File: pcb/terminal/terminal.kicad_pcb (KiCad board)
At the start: 2 copper layers, 34 parts, among them J1 Conn_02x08_Odd_Even, Q1 2N7002, Q2 2N7002, Q3 2N7002, SW1 1, SW10 8, SW11 9, SW13 0, SW2 2, SW3 3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

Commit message: Updates
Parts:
- added C2: 0.1u, Capacitor_SMD:C_0805_2012Metric_Pad1.15x1.40mm_HandSolder, F.Cu at (150.5, 60.0)
- added D14: 1N5818, Diode_THT:D_DO-41_SOD81_P10.16mm_Horizontal, F.Cu at (134.0, 58.0)
- added J2: ISP, Connector_PinHeader_2.54mm:PinHeader_2x03_P2.54mm_Vertical, F.Cu at (154.5, 67.5)
- added U1: ATtiny88, Package_DIP:DIP-28_W7.62mm, F.Cu at (139.5, 42.5)
- C1: value 0.47u -> 47u
- J1: value Conn_02x08_Odd_Even -> Conn_02x15_Odd_Even; footprint Connector_IDC:IDC-Header_2x08_P2.54mm_Vertical -> Connector_IDC:IDC-Header_2x15_P2.54mm_Vertical
- Q1, Q2, Q3: footprint Package_TO_SOT_SMD:SOT-23 -> Package_TO_SOT_SMD:SOT-23_Handsoldering
- moved C1 81.4 mm to (125.0, 78.0), turned to 0 degrees
- moved Q1 68.2 mm to (95.0, 79.5)
- moved R1 68.2 mm to (95.0, 74.5)
- moved RV1 67.5 mm to (83.5, 80.0)
- moved DS1 61.4 mm to (89.0, 86.0)
- moved J1 61.0 mm to (124.0, 64.0)
- moved Q2 59.1 mm to (88.0, 124.5)
- moved Q3 59.1 mm to (88.0, 130.5)
- moved D1 58.3 mm to (104.0, 130.5)
- moved D10 58.3 mm to (94.0, 130.5)
- moved D11 58.3 mm to (138.0, 130.5)
- moved D12 58.3 mm to (148.0, 130.5)
- moved D13 58.3 mm to (94.0, 122.5)
- moved D2 58.3 mm to (114.0, 130.5)
- moved D3 58.3 mm to (124.0, 130.5)
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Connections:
- DS1 pad 6: WR -> WR_TERM
- J1 pad 10: D5 -> D7
- J1 pad 11: D4 -> A6
- J1 pad 12: D3 -> D6
- J1 pad 13: D2 -> A5
- J1 pad 14: D1 -> D5
- J1 pad 15: D0 -> A4
- J1 pad 16: GND -> D4
- J1 pad 2: WR -> D11
- J1 pad 3: RD -> (no net)
- J1 pad 4: D11 -> D10
- J1 pad 5: D10 -> (no net)
- J1 pad 7: D8 -> A8
- J1 pad 8: D7 -> D8
- J1 pad 9: D6 -> A7
- Q2 pad 1: RD -> RD_TERM
- Q3 pad 1: RD -> RD_TERM

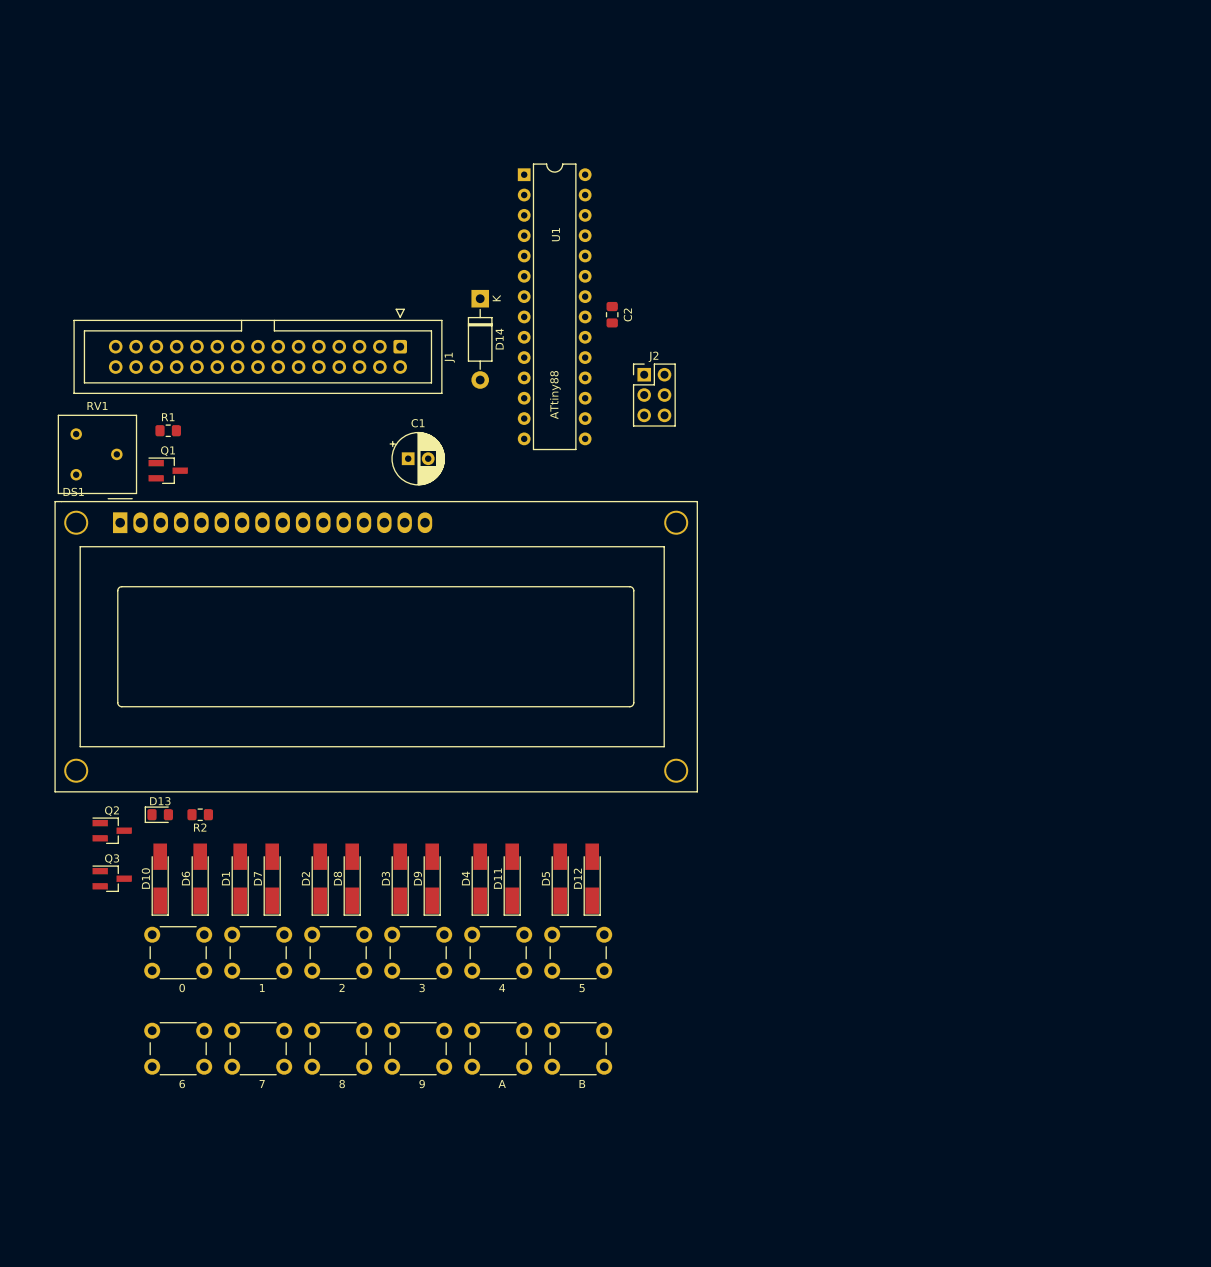
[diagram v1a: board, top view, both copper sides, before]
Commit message: Add some assembler directives.
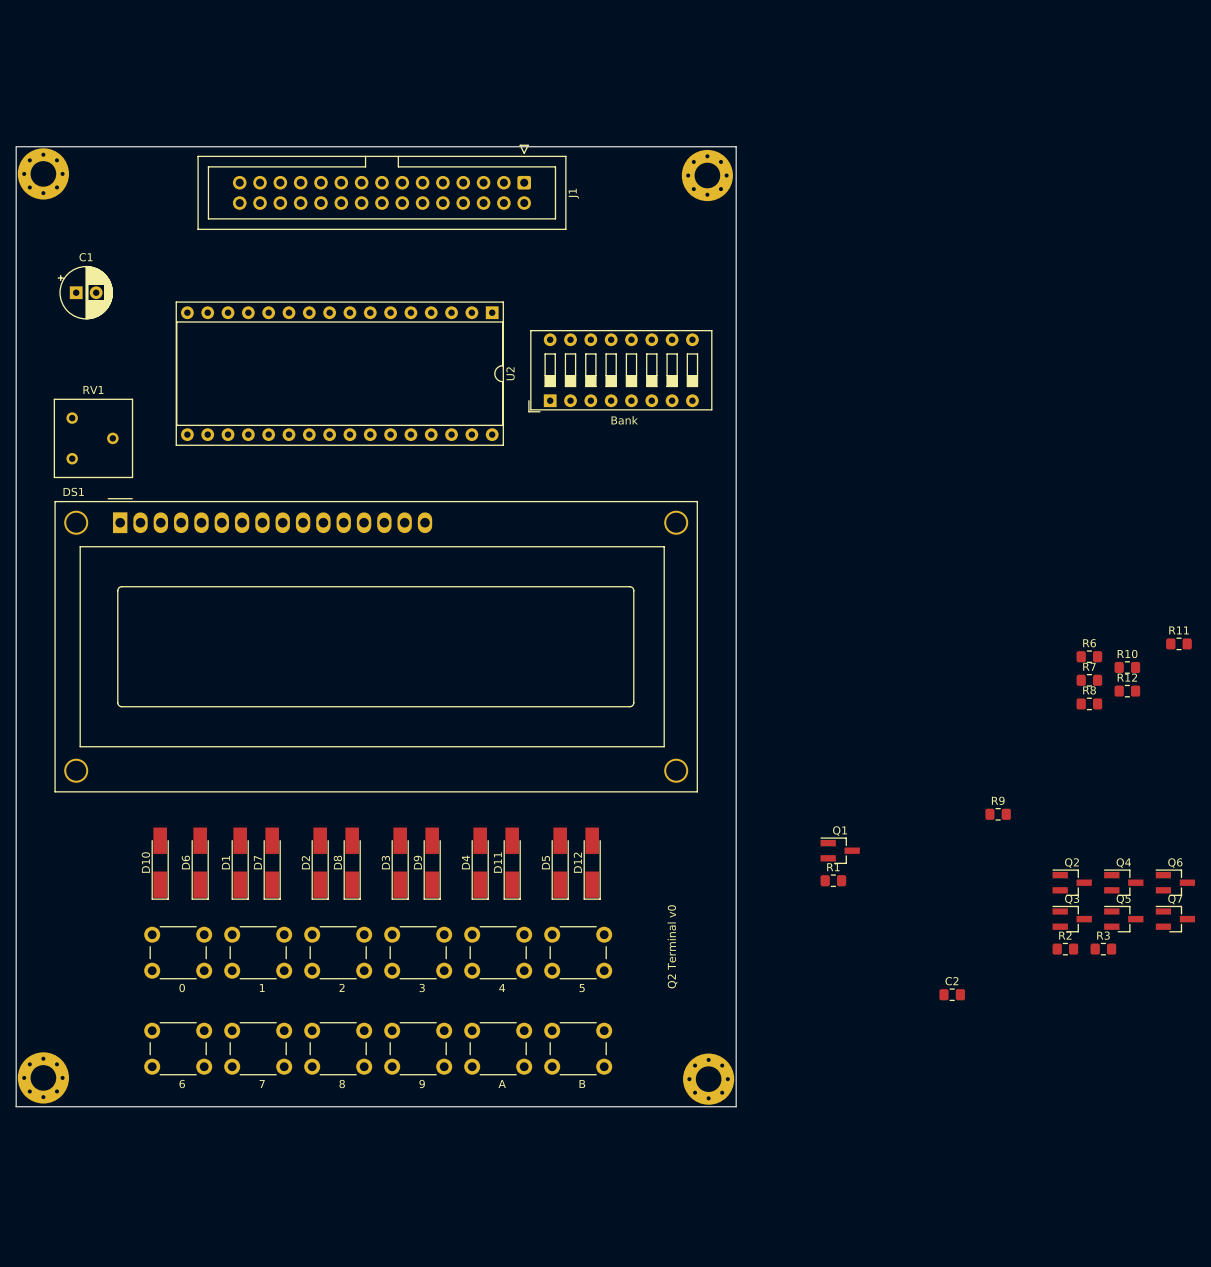
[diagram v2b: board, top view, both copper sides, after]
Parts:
- removed D13: RD, Diode_SMD:D_0805_2012Metric_Pad1.15x1.40mm_HandSolder
- removed D14: 1N5818, Diode_THT:D_DO-41_SOD81_P10.16mm_Horizontal
- removed J2: ISP, Connector_PinHeader_2.54mm:PinHeader_2x03_P2.54mm_Vertical
- removed U1: ATtiny88, Package_DIP:DIP-28_W7.62mm
- added H1: MountingHole_Pad, MountingHole:MountingHole_3.2mm_M3_Pad_Via, F.Cu at (79.4, 42.4)
- added H2: MountingHole_Pad, MountingHole:MountingHole_3.2mm_M3_Pad_Via, F.Cu at (79.4, 155.4)
- added H3: MountingHole_Pad, MountingHole:MountingHole_3.2mm_M3_Pad_Via, F.Cu at (162.4, 42.6)
- added H4: MountingHole_Pad, MountingHole:MountingHole_3.2mm_M3_Pad_Via, F.Cu at (162.6, 155.6)
- added Q4: 2N7002, Package_TO_SOT_SMD:SOT-23_Handsoldering, F.Cu at (214.4, 131.0)
- added Q5: 2N7002, Package_TO_SOT_SMD:SOT-23_Handsoldering, F.Cu at (214.4, 135.6)
- added Q6: 2N7002, Package_TO_SOT_SMD:SOT-23_Handsoldering, F.Cu at (220.9, 131.0)
- added Q7: 2N7002, Package_TO_SOT_SMD:SOT-23_Handsoldering, F.Cu at (220.9, 135.6)
- added R10: 10k, Resistor_SMD:R_0805_2012Metric_Pad1.15x1.40mm_HandSolder, F.Cu at (214.9, 104.1)
- added R11: 10k, Resistor_SMD:R_0805_2012Metric_Pad1.15x1.40mm_HandSolder, F.Cu at (221.3, 101.2)
- added R12: 10k, Resistor_SMD:R_0805_2012Metric_Pad1.15x1.40mm_HandSolder, F.Cu at (214.9, 107.0)
- added R3: 10k, Resistor_SMD:R_0805_2012Metric_Pad1.15x1.40mm_HandSolder, F.Cu at (211.9, 139.3)
- added R6: 10k, Resistor_SMD:R_0805_2012Metric_Pad1.15x1.40mm_HandSolder, F.Cu at (210.2, 102.8)
- added R7: 10k, Resistor_SMD:R_0805_2012Metric_Pad1.15x1.40mm_HandSolder, F.Cu at (210.2, 105.7)
- added R8: 10k, Resistor_SMD:R_0805_2012Metric_Pad1.15x1.40mm_HandSolder, F.Cu at (210.2, 108.7)
- added R9: 10k, Resistor_SMD:R_0805_2012Metric_Pad1.15x1.40mm_HandSolder, F.Cu at (198.7, 122.5)
- added SW12: Bank, Button_Switch_THT:SW_DIP_SPSTx08_Slide_9.78x22.5mm_W7.62mm_P2.54mm, F.Cu at (142.8, 70.8)
- added U2: SST39SF040, Package_DIP:DIP-32_W15.24mm_Socket, F.Cu at (135.5, 59.8)
- moved Q2 120.2 mm to (208.0, 131.0)
- moved Q3 120.1 mm to (208.0, 135.6)
- moved R2 109.4 mm to (207.2, 139.3), turned to 0 degrees
- moved R1 100.4 mm to (178.2, 130.8)
- moved Q1 96.5 mm to (179.0, 127.0)
- moved C2 95.0 mm to (193.0, 145.0), turned to 0 degrees
- moved C1 46.4 mm to (83.5, 57.2)
- moved J1 25.7 mm to (139.5, 43.5)
- moved RV1 2.06 mm to (83.0, 78.0)
- moved D1 2.00 mm to (104.0, 128.5)
- moved D10 2.00 mm to (94.0, 128.5)
- moved D11 2.00 mm to (138.0, 128.5)
- moved D12 2.00 mm to (148.0, 128.5)
- moved D2 2.00 mm to (114.0, 128.5)
- moved D3 2.00 mm to (124.0, 128.5)
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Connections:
- C2 pad 1: AT_VCC -> VCC
- J1 pad 25: WR_DISK -> (no net)
- J1 pad 3: (no net) -> A10
- J1 pad 5: (no net) -> A9
- Q1 pad 1: D8 -> RD_DISK
- Q1 pad 3: Net-(DS1-Pad4) -> Net-(Q1-Pad3)
- Q2 pad 1: RD_TERM -> D8
- Q2 pad 3: Net-(D13-Pad1) -> Net-(DS1-Pad4)
- Q3 pad 1: RD_TERM -> RD_DISK
- Q3 pad 3: Net-(Q3-Pad3) -> D8
- R1 pad 2: Net-(DS1-Pad4) -> Net-(Q1-Pad3)
- R2 pad 2: Net-(D13-Pad2) -> Net-(DS1-Pad4)
- SW1 pad 1: Net-(Q3-Pad3) -> Net-(Q7-Pad3)
- SW10 pad 1: Net-(Q3-Pad3) -> Net-(Q7-Pad3)
- SW11 pad 1: Net-(Q3-Pad3) -> Net-(Q7-Pad3)
- SW13 pad 1: Net-(Q3-Pad3) -> Net-(Q7-Pad3)
- SW2 pad 1: Net-(Q3-Pad3) -> Net-(Q7-Pad3)
- SW3 pad 1: Net-(Q3-Pad3) -> Net-(Q7-Pad3)
- SW4 pad 1: Net-(Q3-Pad3) -> Net-(Q7-Pad3)
- SW5 pad 1: Net-(Q3-Pad3) -> Net-(Q7-Pad3)
- SW6 pad 1: Net-(Q3-Pad3) -> Net-(Q7-Pad3)
- SW7 pad 1: Net-(Q3-Pad3) -> Net-(Q7-Pad3)
- SW8 pad 1: Net-(Q3-Pad3) -> Net-(Q7-Pad3)
- SW9 pad 1: Net-(Q3-Pad3) -> Net-(Q7-Pad3)
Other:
- board outline added: 90 x 120 mm
- board text added: "Q2 Terminal v0"

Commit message: Terminal
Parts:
- removed Q1, Q2, Q3, Q4, Q5, Q6, Q7: 2N7002, Package_TO_SOT_SMD:SOT-23_Handsoldering
- removed R10, R11, R12, R3, R6, R7, R8, R9: 10k, Resistor_SMD:R_0805_2012Metric_Pad1.15x1.40mm_HandSolder
- removed SW12: Bank, Button_Switch_THT:SW_DIP_SPSTx08_Slide_9.78x22.5mm_W7.62mm_P2.54mm
- added C3: 0.1u, Capacitor_SMD:C_0805_2012Metric_Pad1.15x1.40mm_HandSolder, F.Cu at (103.0, 52.0)
- added C4: 0.1u, Capacitor_SMD:C_0805_2012Metric_Pad1.15x1.40mm_HandSolder, F.Cu at (94.0, 84.0)
- added D13: LED, LED_THT:LED_D3.0mm, F.Cu at (158.2, 146.5)
- added U1: 28C256, Package_DIP:DIP-28_W15.24mm_Socket, F.Cu at (156.0, 74.0)
- added U3: 574, Package_SO:SOIC-20W_7.5x12.8mm_P1.27mm, F.Cu at (112.0, 56.0)
- added U4: 574, Package_SO:SOIC-20W_7.5x12.8mm_P1.27mm, F.Cu at (137.5, 56.0)
- D1, D10, D11, D12, D2, D3, D4, D5, D6, D7, D8, D9: footprint Diode_SMD:D_MiniMELF_Handsoldering -> Diode_SMD:D_SOD-123
- R1: value 10k -> 1k
- U2: value SST39SF040 -> 14; footprint Package_DIP:DIP-32_W15.24mm_Socket -> Package_SO:SOIC-14_3.9x8.7mm_P1.27mm
- moved C2 93.7 mm to (151.5, 61.0), turned to 90 degrees
- moved R1 91.3 mm to (97.5, 88.0)
- moved RV1 71.6 mm to (85.8, 149.5)
- moved R2 44.0 mm to (163.8, 146.2), turned to 270 degrees
- moved U2 41.5 mm to (100.5, 82.0), turned to 90 degrees
- moved H2 18.6 mm to (83.4, 173.6)
- moved D1 18.4 mm to (108.0, 146.5)
- moved D10 18.4 mm to (98.0, 146.5)
- moved D11 18.4 mm to (142.0, 146.5)
- moved D12 18.4 mm to (152.0, 146.5)
- moved D2 18.4 mm to (118.0, 146.5)
- moved D3 18.4 mm to (128.0, 146.5)
- moved D4 18.4 mm to (138.0, 146.5)
- moved D5 18.4 mm to (148.0, 146.5)
- moved D6 18.4 mm to (103.0, 146.5)
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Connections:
- R1 pad 1: VCC -> Net-(C4-Pad1)
- R1 pad 2: Net-(Q1-Pad3) -> Net-(R1-Pad2)
- R2 pad 2: Net-(DS1-Pad4) -> Net-(D13-Pad2)
- SW1 pad 1: Net-(Q7-Pad3) -> Net-(D13-Pad1)
- SW10 pad 1: Net-(Q7-Pad3) -> Net-(D13-Pad1)
- SW11 pad 1: Net-(Q7-Pad3) -> Net-(D13-Pad1)
- SW13 pad 1: Net-(Q7-Pad3) -> Net-(D13-Pad1)
- SW2 pad 1: Net-(Q7-Pad3) -> Net-(D13-Pad1)
- SW3 pad 1: Net-(Q7-Pad3) -> Net-(D13-Pad1)
- SW4 pad 1: Net-(Q7-Pad3) -> Net-(D13-Pad1)
- SW5 pad 1: Net-(Q7-Pad3) -> Net-(D13-Pad1)
- SW6 pad 1: Net-(Q7-Pad3) -> Net-(D13-Pad1)
- SW7 pad 1: Net-(Q7-Pad3) -> Net-(D13-Pad1)
- SW8 pad 1: Net-(Q7-Pad3) -> Net-(D13-Pad1)
- SW9 pad 1: Net-(Q7-Pad3) -> Net-(D13-Pad1)
- U2 pad 1: B7 -> Net-(C4-Pad1)
- U2 pad 10: A2 -> Net-(U2-Pad10)
- U2 pad 11: A1 -> RD_DISK
- U2 pad 12: A0 -> Net-(D13-Pad1)
- U2 pad 13: D0 -> RD_TERM
- U2 pad 14: D1 -> VCC
- U2 pad 2: B5 -> Net-(R1-Pad2)
- U2 pad 3: B4 -> Net-(R1-Pad2)
- U2 pad 4: B1 -> Net-(U1-Pad10)
- U2 pad 5: A7 -> Net-(U1-Pad10)
- U2 pad 6: A6 -> Net-(U2-Pad6)
- U2 pad 7: A5 -> GND
- U2 pad 8: A4 -> Net-(DS1-Pad4)
- U2 pad 9: A3 -> D8
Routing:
- net GND: track 0.00 -> 556.3 mm, vias 0 -> 7
- net VCC: track 0.00 -> 335.9 mm
- net Net-(D13-Pad1): track 0.00 -> 214.8 mm, vias 0 -> 1
- net D6: track 0.00 -> 164.7 mm, vias 0 -> 7
- net D8: track 0.00 -> 161.6 mm, vias 0 -> 5
- net D7: track 0.00 -> 154.6 mm, vias 0 -> 6
- net D5: track 0.00 -> 144.6 mm, vias 0 -> 4
- net D4: track 0.00 -> 138.5 mm, vias 0 -> 4
- net D9: track 0.00 -> 132.5 mm, vias 0 -> 3
- net D3: track 0.00 -> 131.9 mm, vias 0 -> 4
- net D10: track 0.00 -> 128.4 mm, vias 0 -> 3
- net D11: track 0.00 -> 127.5 mm, vias 0 -> 3
- net D2: track 0.00 -> 125.8 mm, vias 0 -> 4
- net D0: track 0.00 -> 122.8 mm, vias 0 -> 4
- net D1: track 0.00 -> 122.0 mm, vias 0 -> 4
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- added copper zone on B.Cu, net GND
- added copper zone on F.Cu, net GND
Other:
- board size 90 x 120 mm -> 90 x 150 mm
